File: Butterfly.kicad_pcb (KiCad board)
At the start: 2 copper layers, 93.1 x 65.5 mm, 34 parts, among them J1 Conn_02x03_Odd_Even, J2 USB_A, U1 ATTINY85-20PU

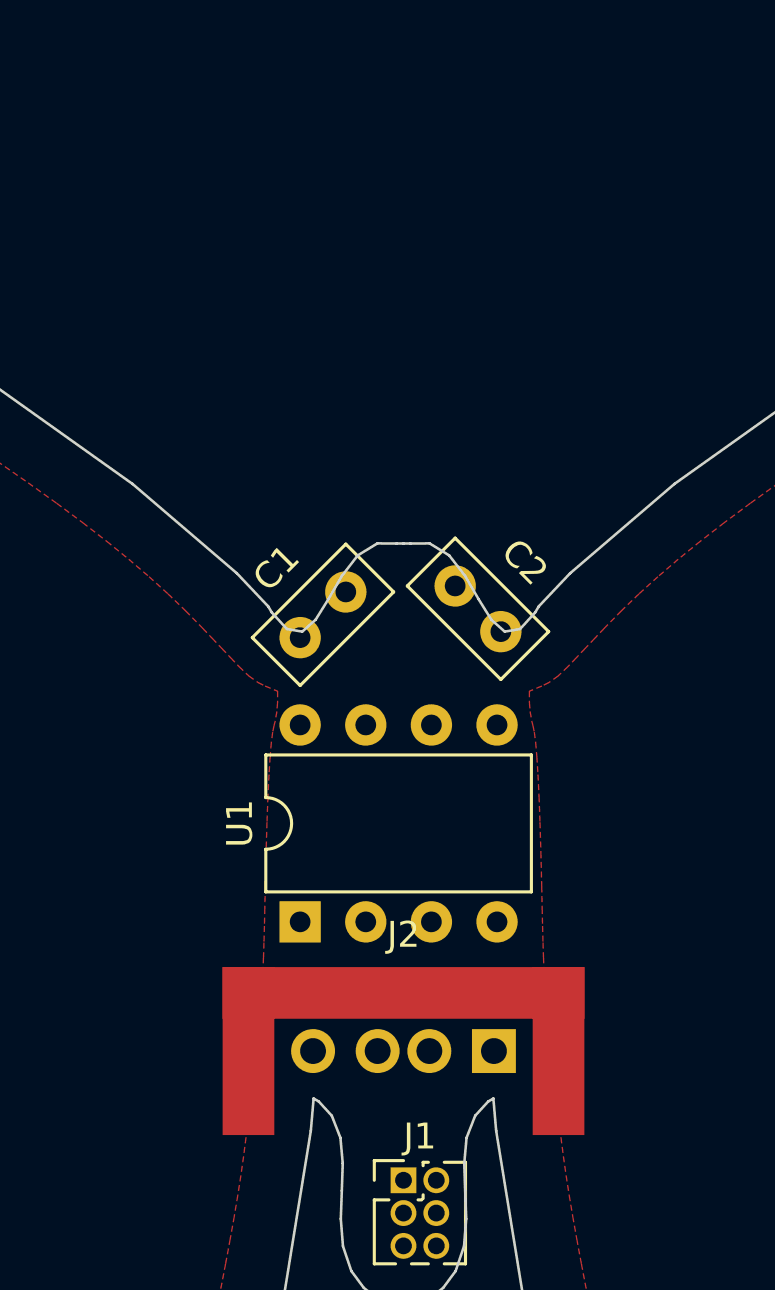
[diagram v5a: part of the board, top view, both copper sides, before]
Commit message: Seeing how much can fit on the body.
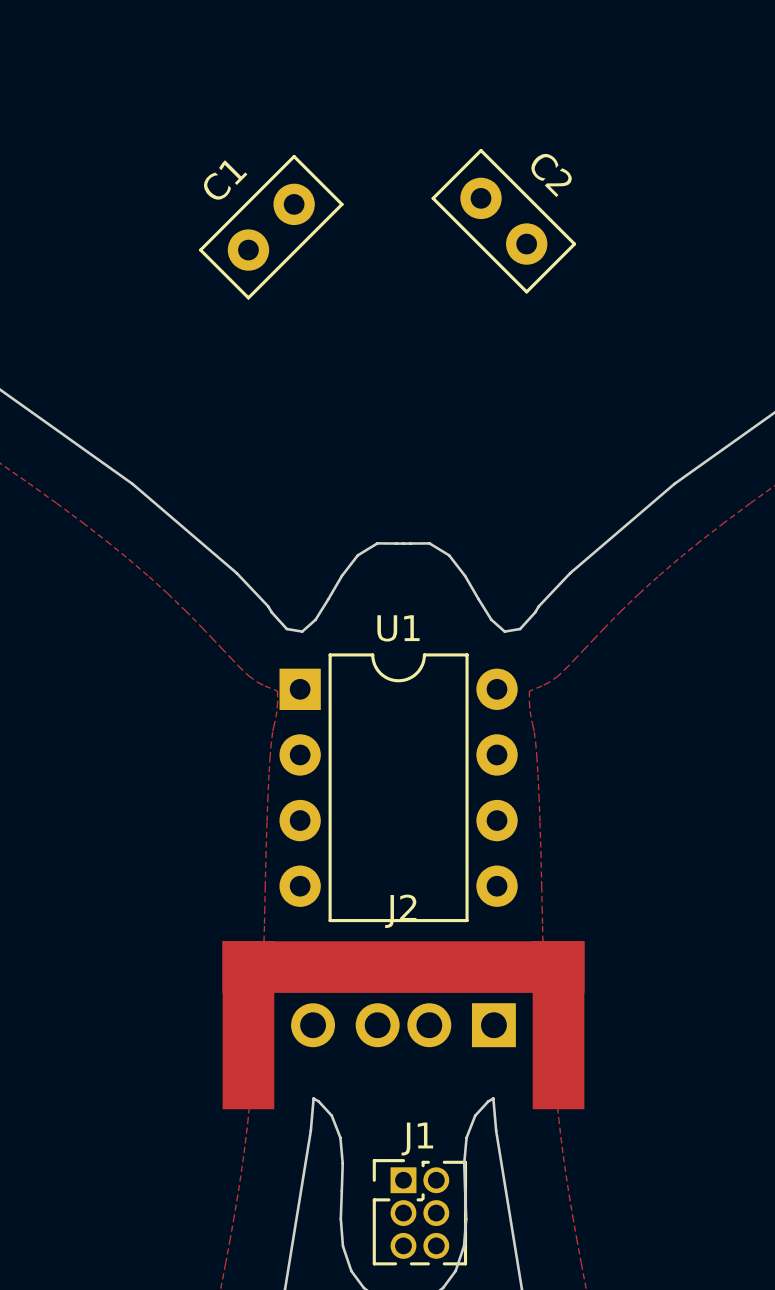
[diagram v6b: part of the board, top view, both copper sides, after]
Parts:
- moved C1 15.1 mm to (139.0, 77.0)
- moved C2 15.0 mm to (148.0, 75.0)
- moved U1 9.00 mm to (141.0, 94.0), turned to 0 degrees
- moved J2 1.00 mm to (145.0, 107.0)
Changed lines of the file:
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@@
   )
   (module Capacitors_THT:C_Disc_D5.0mm_W2.5mm_P2.50mm (layer F.Cu)
-    (at 141 92 45)
+    (at 139 77 45)
     (descr "C, Disc series, Radial, pin pitch=2.50mm, , diameter*width=5*2.5mm^2, Capacitor, http://cdn-reichelt.de/documents/datenblatt/B300/DS_KERKO_TC.pdf")
     (tags "C Disc series Radial pin pitch 2.50mm  diameter 5mm width 2.5mm Capacitor")
@@
   )
   (module Capacitors_THT:C_Disc_D5.0mm_W2.5mm_P2.50mm (layer F.Cu)
-    (at 147 90 315)
+    (at 148 75 315)
     (descr "C, Disc series, Radial, pin pitch=2.50mm, , diameter*width=5*2.5mm^2, Capacitor, http://cdn-reichelt.de/documents/datenblatt/B300/DS_KERKO_TC.pdf")
     (tags "C Disc series Radial pin pitch 2.50mm  diameter 5mm width 2.5mm Capacitor")
@@
   )
   (module myLibrary:USB_A_Molex-0480370001_Vertical (layer F.Cu)
-    (at 145 108)
+    (at 145 107)
     (descr "USB A plug, through-hole, vertical, http://www.molex.com/pdm_docs/sd/480370001_sd.pdf")
     (tags "usb plug vertical")
@@
   )
   (module Housings_DIP:DIP-8_W7.62mm (layer F.Cu)
-    (at 141 103 90)
+    (at 141 94)
     (descr "8-lead though-hole mounted DIP package, row spacing 7.62 mm (300 mils)")
     (tags "THT DIP DIL PDIP 2.54mm 7.62mm 300mil")
-    (fp_text reference U1 (at 3.81 -2.33 90) (layer F.SilkS)
-      (effects (font (size 1 1) (thickness 0.15)))
-    )
-    (fp_text value ATTINY85-20PU (at 3.81 9.95 90) (layer F.Fab)
+    (fp_text reference U1 (at 3.81 -2.33) (layer F.SilkS)
+      (effects (font (size 1 1) (thickness 0.15)))
+    )
+    (fp_text value ATTINY85-20PU (at 3.81 9.95) (layer F.Fab)
       (effects (font (size 1 1) (thickness 0.15)))
     )
@@
     (fp_line (start 8.7 9.15) (end 8.7 -1.55) (layer F.CrtYd) (width 0.05))
     (fp_line (start 8.7 -1.55) (end -1.1 -1.55) (layer F.CrtYd) (width 0.05))
-    (fp_text user %R (at 3.81 3.81 90) (layer F.Fab)
-      (effects (font (size 1 1) (thickness 0.15)))
-    )
-    (pad 1 thru_hole rect (at 0 0 90) (size 1.6 1.6) (drill 0.8) (layers *.Cu *.Mask)
+    (fp_text user %R (at 3.81 3.81) (layer F.Fab)
+      (effects (font (size 1 1) (thickness 0.15)))
+    )
+    (pad 1 thru_hole rect (at 0 0) (size 1.6 1.6) (drill 0.8) (layers *.Cu *.Mask)
       (net 31 "Net-(J1-Pad5)"))
-    (pad 5 thru_hole oval (at 7.62 7.62 90) (size 1.6 1.6) (drill 0.8) (layers *.Cu *.Mask)
+    (pad 5 thru_hole oval (at 7.62 7.62) (size 1.6 1.6) (drill 0.8) (layers *.Cu *.Mask)
       (net 30 "Net-(J1-Pad4)"))
-    (pad 2 thru_hole oval (at 0 2.54 90) (size 1.6 1.6) (drill 0.8) (layers *.Cu *.Mask)
+    (pad 2 thru_hole oval (at 0 2.54) (size 1.6 1.6) (drill 0.8) (layers *.Cu *.Mask)
       (net 34 "Net-(R1-Pad2)"))
-    (pad 6 thru_hole oval (at 7.62 5.08 90) (size 1.6 1.6) (drill 0.8) (layers *.Cu *.Mask)
+    (pad 6 thru_hole oval (at 7.62 5.08) (size 1.6 1.6) (drill 0.8) (layers *.Cu *.Mask)
       (net 28 "Net-(J1-Pad1)"))
-    (pad 3 thru_hole oval (at 0 5.08 90) (size 1.6 1.6) (drill 0.8) (layers *.Cu *.Mask)
+    (pad 3 thru_hole oval (at 0 5.08) (size 1.6 1.6) (drill 0.8) (layers *.Cu *.Mask)
       (net 35 "Net-(RV1-Pad2)"))
-    (pad 7 thru_hole oval (at 7.62 2.54 90) (size 1.6 1.6) (drill 0.8) (layers *.Cu *.Mask)
+    (pad 7 thru_hole oval (at 7.62 2.54) (size 1.6 1.6) (drill 0.8) (layers *.Cu *.Mask)
       (net 29 "Net-(J1-Pad3)"))
-    (pad 4 thru_hole oval (at 0 7.62 90) (size 1.6 1.6) (drill 0.8) (layers *.Cu *.Mask)
-      (net 2 GND))
-    (pad 8 thru_hole oval (at 7.62 0 90) (size 1.6 1.6) (drill 0.8) (layers *.Cu *.Mask)
+    (pad 4 thru_hole oval (at 0 7.62) (size 1.6 1.6) (drill 0.8) (layers *.Cu *.Mask)
+      (net 2 GND))
+    (pad 8 thru_hole oval (at 7.62 0) (size 1.6 1.6) (drill 0.8) (layers *.Cu *.Mask)
       (net 1 +5V))
     (model ${KISYS3DMOD}/Housings_DIP.3dshapes/DIP-8_W7.62mm.wrl

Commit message: Position LED footprints.
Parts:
- moved D3 76.1 mm to (107.0, 79.0)
- moved D12 74.2 mm to (179.0, 79.0)
- moved D6 64.6 mm to (108.0, 92.0)
- moved D2 62.6 mm to (119.0, 88.0)
- moved D15 62.4 mm to (178.0, 92.0)
- moved D11 62.3 mm to (168.0, 87.0)
- moved D5 52.3 mm to (120.0, 99.0)
- moved D1 51.9 mm to (131.0, 95.0)
- moved D10 50.9 mm to (155.0, 95.0)
- moved D14 50.5 mm to (166.0, 99.0)
- moved D4 42.9 mm to (132.0, 104.0)
- moved D13 41.9 mm to (154.0, 104.0)
- moved D7 41.6 mm to (124.0, 109.0)
- moved D16 39.7 mm to (162.0, 109.0)
- moved D8 32.6 mm to (120.0, 124.0)
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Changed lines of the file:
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@@
   (general
     (links 93)
-    (no_connects 47)
+    (no_connects 83)
     (area 98.409153 69.322099 191.590847 155.950641)
     (thickness 1.6)
@@
   )
   (module LEDs:LED_D5.0mm-4 (layer F.Cu)
-    (at 145 144.925641)
+    (at 131 95)
     (descr "LED, diameter 5.0mm, 2 pins, diameter 5.0mm, 3 pins, diameter 5.0mm, 4 pins, http://www.kingbright.com/attachments/file/psearch/000/00/00/L-154A4SUREQBFZGEW(Ver.9A).pdf")
     (tags "LED diameter 5.0mm 2 pins diameter 5.0mm 3 pins diameter 5.0mm 4 pins")
@@
   )
   (module LEDs:LED_D5.0mm-4 (layer F.Cu)
-    (at 145 144.925641)
+    (at 119 88)
     (descr "LED, diameter 5.0mm, 2 pins, diameter 5.0mm, 3 pins, diameter 5.0mm, 4 pins, http://www.kingbright.com/attachments/file/psearch/000/00/00/L-154A4SUREQBFZGEW(Ver.9A).pdf")
     (tags "LED diameter 5.0mm 2 pins diameter 5.0mm 3 pins diameter 5.0mm 4 pins")
@@
   )
   (module LEDs:LED_D5.0mm-4 (layer F.Cu)
-    (at 145 144.925641)
+    (at 107 79)
     (descr "LED, diameter 5.0mm, 2 pins, diameter 5.0mm, 3 pins, diameter 5.0mm, 4 pins, http://www.kingbright.com/attachments/file/psearch/000/00/00/L-154A4SUREQBFZGEW(Ver.9A).pdf")
     (tags "LED diameter 5.0mm 2 pins diameter 5.0mm 3 pins diameter 5.0mm 4 pins")
@@
   )
   (module LEDs:LED_D5.0mm-4 (layer F.Cu)
-    (at 145 144.925641)
+    (at 132 104)
     (descr "LED, diameter 5.0mm, 2 pins, diameter 5.0mm, 3 pins, diameter 5.0mm, 4 pins, http://www.kingbright.com/attachments/file/psearch/000/00/00/L-154A4SUREQBFZGEW(Ver.9A).pdf")
     (tags "LED diameter 5.0mm 2 pins diameter 5.0mm 3 pins diameter 5.0mm 4 pins")
@@
   )
   (module LEDs:LED_D5.0mm-4 (layer F.Cu)
-    (at 145 144.925641)
+    (at 120 99)
     (descr "LED, diameter 5.0mm, 2 pins, diameter 5.0mm, 3 pins, diameter 5.0mm, 4 pins, http://www.kingbright.com/attachments/file/psearch/000/00/00/L-154A4SUREQBFZGEW(Ver.9A).pdf")
     (tags "LED diameter 5.0mm 2 pins diameter 5.0mm 3 pins diameter 5.0mm 4 pins")
@@
   )
   (module LEDs:LED_D5.0mm-4 (layer F.Cu)
-    (at 145 144.925641)
+    (at 108 92)
     (descr "LED, diameter 5.0mm, 2 pins, diameter 5.0mm, 3 pins, diameter 5.0mm, 4 pins, http://www.kingbright.com/attachments/file/psearch/000/00/00/L-154A4SUREQBFZGEW(Ver.9A).pdf")
     (tags "LED diameter 5.0mm 2 pins diameter 5.0mm 3 pins diameter 5.0mm 4 pins")
@@
   )
   (module LEDs:LED_D5.0mm-4 (layer F.Cu)
-    (at 145 144.925641)
+    (at 124 109)
     (descr "LED, diameter 5.0mm, 2 pins, diameter 5.0mm, 3 pins, diameter 5.0mm, 4 pins, http://www.kingbright.com/attachments/file/psearch/000/00/00/L-154A4SUREQBFZGEW(Ver.9A).pdf")
     (tags "LED diameter 5.0mm 2 pins diameter 5.0mm 3 pins diameter 5.0mm 4 pins")
@@
   )
   (module LEDs:LED_D5.0mm-4 (layer F.Cu)
-    (at 145 144.925641)
+    (at 120 124)
     (descr "LED, diameter 5.0mm, 2 pins, diameter 5.0mm, 3 pins, diameter 5.0mm, 4 pins, http://www.kingbright.com/attachments/file/psearch/000/00/00/L-154A4SUREQBFZGEW(Ver.9A).pdf")
     (tags "LED diameter 5.0mm 2 pins diameter 5.0mm 3 pins diameter 5.0mm 4 pins")
@@
   )
   (module LEDs:LED_D5.0mm-4 (layer F.Cu)
-    (at 145 144.925641)
+    (at 129 119)
     (descr "LED, diameter 5.0mm, 2 pins, diameter 5.0mm, 3 pins, diameter 5.0mm, 4 pins, http://www.kingbright.com/attachments/file/psearch/000/00/00/L-154A4SUREQBFZGEW(Ver.9A).pdf")
     (tags "LED diameter 5.0mm 2 pins diameter 5.0mm 3 pins diameter 5.0mm 4 pins")
@@
   )
   (module LEDs:LED_D5.0mm-4 (layer F.Cu)
-    (at 145 144.925641)
+    (at 155 95)
     (descr "LED, diameter 5.0mm, 2 pins, diameter 5.0mm, 3 pins, diameter 5.0mm, 4 pins, http://www.kingbright.com/attachments/file/psearch/000/00/00/L-154A4SUREQBFZGEW(Ver.9A).pdf")
     (tags "LED diameter 5.0mm 2 pins diameter 5.0mm 3 pins diameter 5.0mm 4 pins")
@@
   )
   (module LEDs:LED_D5.0mm-4 (layer F.Cu)
-    (at 145 144.925641)
+    (at 168 87)
     (descr "LED, diameter 5.0mm, 2 pins, diameter 5.0mm, 3 pins, diameter 5.0mm, 4 pins, http://www.kingbright.com/attachments/file/psearch/000/00/00/L-154A4SUREQBFZGEW(Ver.9A).pdf")
     (tags "LED diameter 5.0mm 2 pins diameter 5.0mm 3 pins diameter 5.0mm 4 pins")
@@
   )
   (module LEDs:LED_D5.0mm-4 (layer F.Cu)
-    (at 145 144.925641)
+    (at 179 79)
     (descr "LED, diameter 5.0mm, 2 pins, diameter 5.0mm, 3 pins, diameter 5.0mm, 4 pins, http://www.kingbright.com/attachments/file/psearch/000/00/00/L-154A4SUREQBFZGEW(Ver.9A).pdf")
     (tags "LED diameter 5.0mm 2 pins diameter 5.0mm 3 pins diameter 5.0mm 4 pins")
@@
   )
   (module LEDs:LED_D5.0mm-4 (layer F.Cu)
-    (at 145 144.925641)
+    (at 154 104)
     (descr "LED, diameter 5.0mm, 2 pins, diameter 5.0mm, 3 pins, diameter 5.0mm, 4 pins, http://www.kingbright.com/attachments/file/psearch/000/00/00/L-154A4SUREQBFZGEW(Ver.9A).pdf")
     (tags "LED diameter 5.0mm 2 pins diameter 5.0mm 3 pins diameter 5.0mm 4 pins")
@@
   )
   (module LEDs:LED_D5.0mm-4 (layer F.Cu)
-    (at 145 144.925641)
+    (at 166 99)
     (descr "LED, diameter 5.0mm, 2 pins, diameter 5.0mm, 3 pins, diameter 5.0mm, 4 pins, http://www.kingbright.com/attachments/file/psearch/000/00/00/L-154A4SUREQBFZGEW(Ver.9A).pdf")
     (tags "LED diameter 5.0mm 2 pins diameter 5.0mm 3 pins diameter 5.0mm 4 pins")
@@
   )
   (module LEDs:LED_D5.0mm-4 (layer F.Cu)
-    (at 145 144.925641)
+    (at 178 92)
     (descr "LED, diameter 5.0mm, 2 pins, diameter 5.0mm, 3 pins, diameter 5.0mm, 4 pins, http://www.kingbright.com/attachments/file/psearch/000/00/00/L-154A4SUREQBFZGEW(Ver.9A).pdf")
     (tags "LED diameter 5.0mm 2 pins diameter 5.0mm 3 pins diameter 5.0mm 4 pins")
@@
   )
   (module LEDs:LED_D5.0mm-4 (layer F.Cu)
-    (at 145 144.925641)
+    (at 162 109)
     (descr "LED, diameter 5.0mm, 2 pins, diameter 5.0mm, 3 pins, diameter 5.0mm, 4 pins, http://www.kingbright.com/attachments/file/psearch/000/00/00/L-154A4SUREQBFZGEW(Ver.9A).pdf")
     (tags "LED diameter 5.0mm 2 pins diameter 5.0mm 3 pins diameter 5.0mm 4 pins")
@@
   )
   (module LEDs:LED_D5.0mm-4 (layer F.Cu)
-    (at 145 144.925641)
+    (at 166 124)
     (descr "LED, diameter 5.0mm, 2 pins, diameter 5.0mm, 3 pins, diameter 5.0mm, 4 pins, http://www.kingbright.com/attachments/file/psearch/000/00/00/L-154A4SUREQBFZGEW(Ver.9A).pdf")
     (tags "LED diameter 5.0mm 2 pins diameter 5.0mm 3 pins diameter 5.0mm 4 pins")
@@
   )
   (module LEDs:LED_D5.0mm-4 (layer F.Cu)
-    (at 145 144.925641)
-    (descr "LED, diameter 5.0mm, 2 pins, diameter 5.0mm, 3 pins, diameter 5.0mm, 4 pins, http://www.kingbright.com/attachments/file/psearch/000/00/00/L-154A4SUREQBFZGEW(Ver.9A).pdf")
-    (tags "LED diameter 5.0mm 2 pins diameter 5.0mm 3 pins diameter 5.0mm 4 pins")
+    (at 157 119)
+    (descr "LED, diameter 5.0mm, 2 pins, diameter 5.0mm, 3 pins, diameter 5.0mm, 4 pins, http://www.kingbright.com/attachments/file/psearch/000/00/00/L-154A4SUREQBFZGEW(Ver.9A).pdf")
+    (tags "LED diameter 5.0mm 2 pins diameter 5.0mm 3 pins diameter 5.0mm 4 pins")

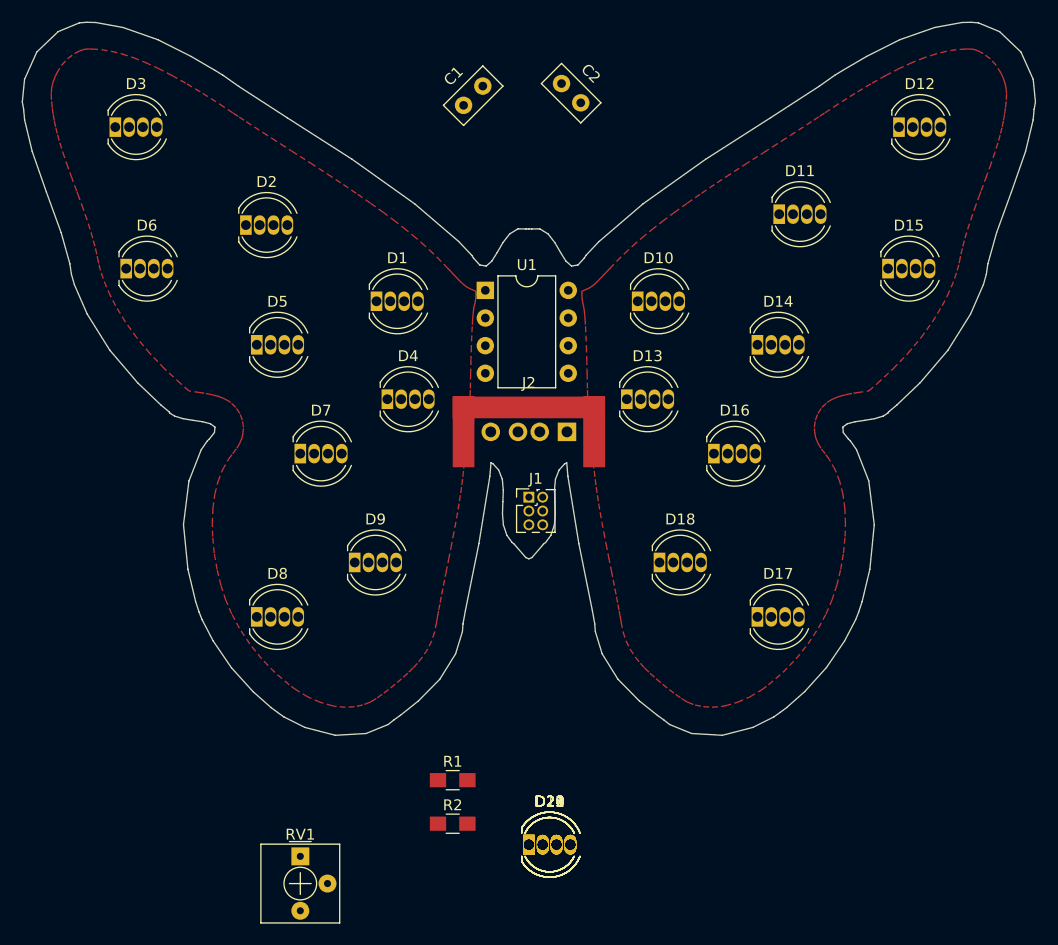
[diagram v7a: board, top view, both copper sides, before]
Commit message: Moved some footprints around.
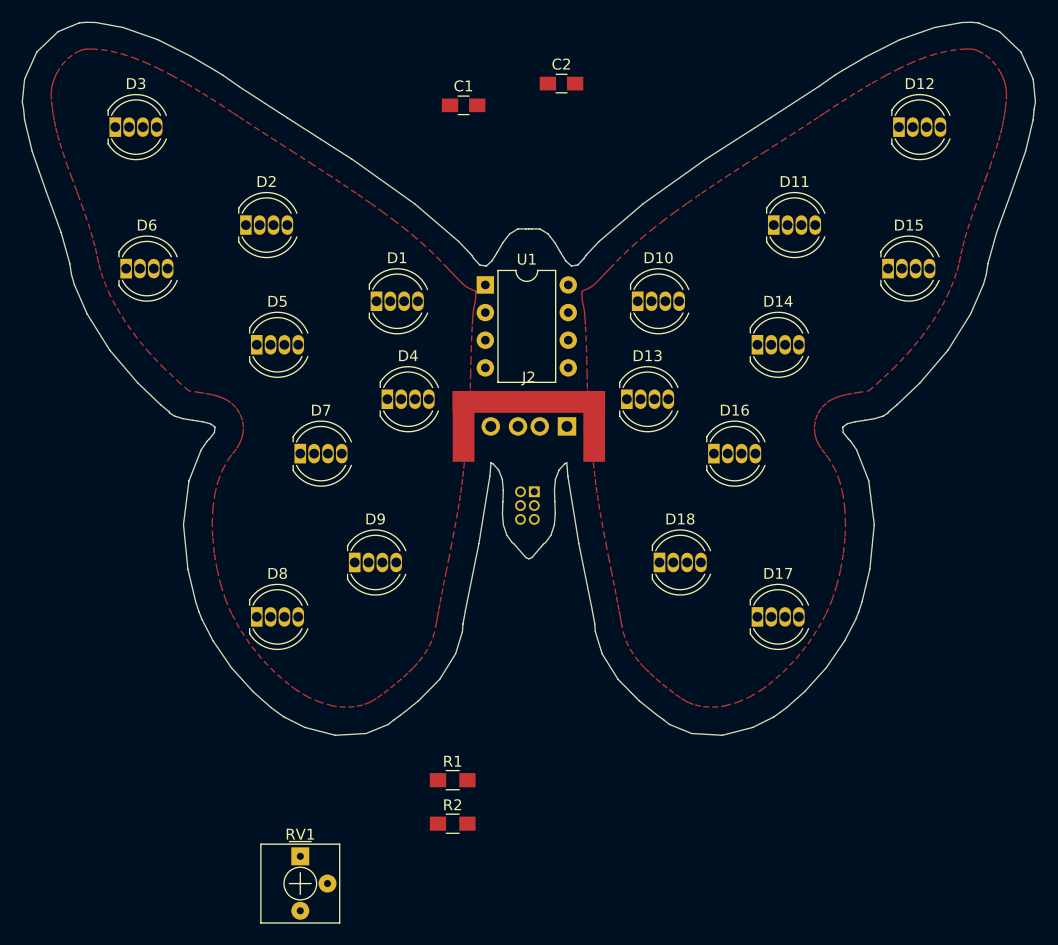
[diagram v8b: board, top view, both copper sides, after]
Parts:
- removed D19, D20, D21, D22, D23, D24: Neopixel_THT, LEDs:LED_D5.0mm-4
- C1: value 4.7uF -> 0.1uF; footprint Capacitors_THT:C_Disc_D5.0mm_W2.5mm_P2.50mm -> Capacitors_SMD:C_0805_HandSoldering
- C2: value 4.7uF -> 10uF; footprint Capacitors_THT:C_Disc_D5.0mm_W2.5mm_P2.50mm -> Capacitors_SMD:C_0805_HandSoldering
- J1: moved to B.Cu
- moved D11 1.12 mm to (167.5, 88.0)
- moved J1 0.71 mm to (145.5, 112.5), turned to 180 degrees
- moved J2 0.50 mm to (145.0, 106.5)
- moved U1 0.50 mm to (141.0, 93.5)
- turned C1 to 0 degrees
- turned C2 to 0 degrees
